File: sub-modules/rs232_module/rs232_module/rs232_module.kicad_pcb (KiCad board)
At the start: 2 copper layers, 50 x 19.4 mm, 12 parts, among them J1 Conn_02x06_Odd_Even, J9 MPT 0,5/ 6-2,54, U1 ADM3312EARUZ-REEL7

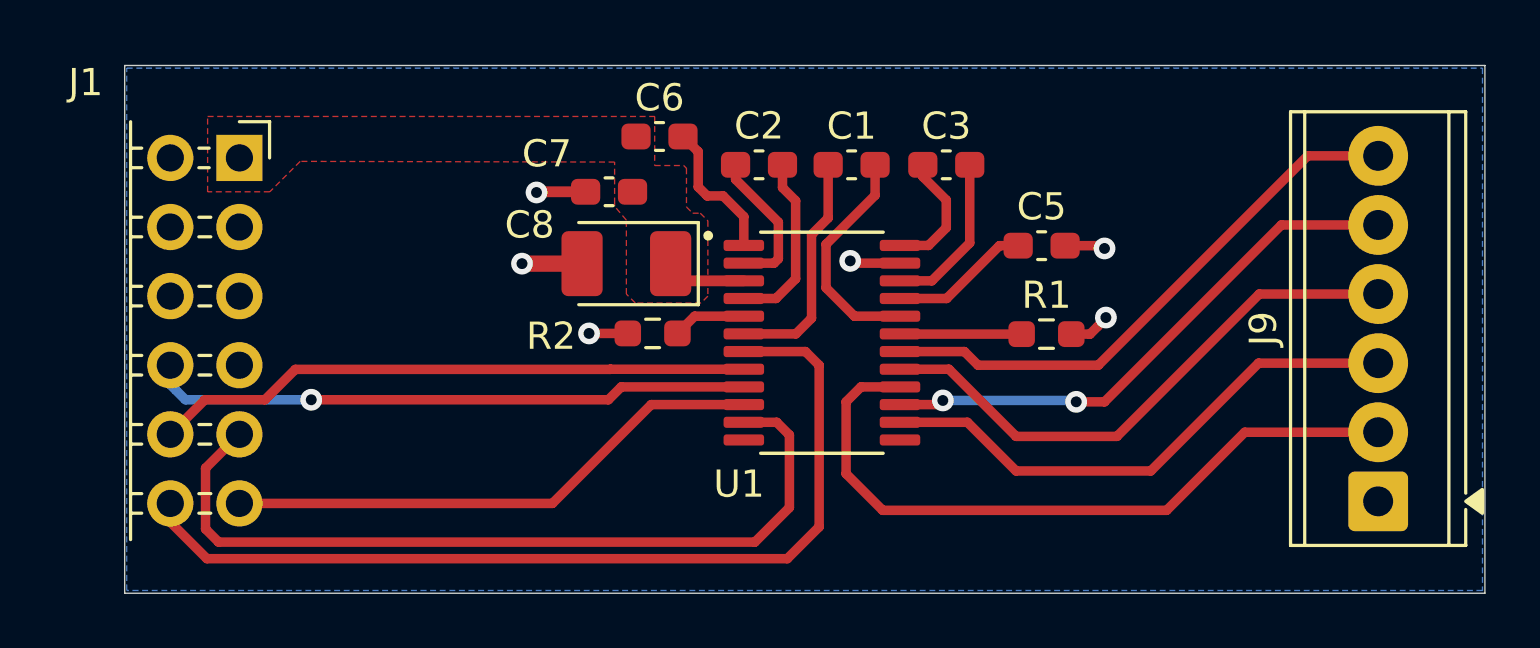
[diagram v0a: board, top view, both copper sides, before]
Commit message: Update schematics after moving to KiCad 10
Added some footprints to a local lib, as the silkscreen caused issues.

Signed-off-by: Marc Kelly <mpkelly@achenar.co.uk>
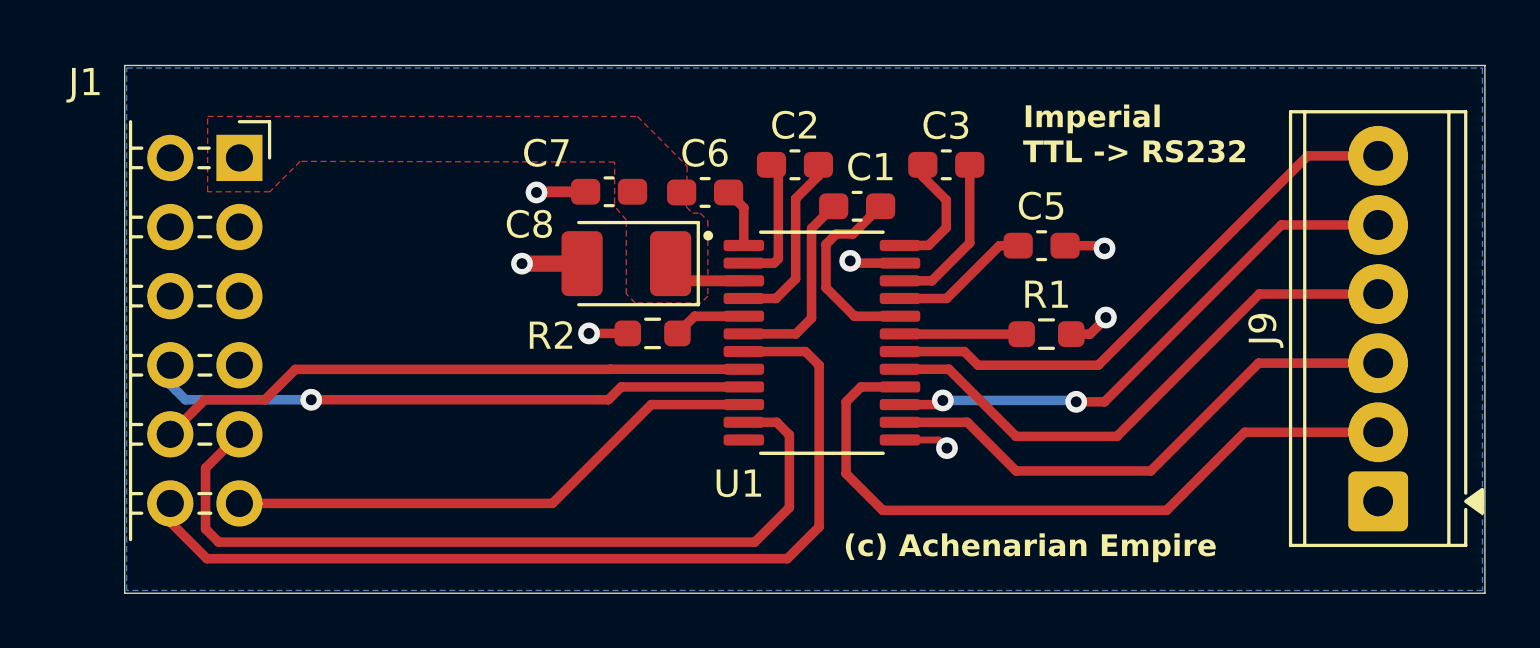
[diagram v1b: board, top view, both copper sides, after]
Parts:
- moved C6 2.65 mm to (142.7, 61.5)
- moved C1 1.54 mm to (148.3, 62.0)
- moved C2 1.32 mm to (146.0, 60.5)
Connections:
- U1 pad 13: unconnected-(U1-R3IN-Pad13) -> GND
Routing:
- net Net-(U1-V+): track 5.27 -> 2.18 mm
- net GND: track 10.3 -> 12.2 mm, vias 6 -> 7
- net Net-(U1-C1+): track 8.62 -> 7.18 mm
- net Net-(U1-C1-): track 8.42 -> 7.33 mm
- net Net-(U1-C2+): track 5.44 -> 4.89 mm
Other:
- board text added: "(c) Achenarian Empire"
- board text added: "Imperial TTL -> RS232"
